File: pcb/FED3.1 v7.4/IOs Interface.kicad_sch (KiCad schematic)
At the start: 29 parts, among them IC1 MC74VHC1GT125DBVT1G, Q2 DMP2035U-7

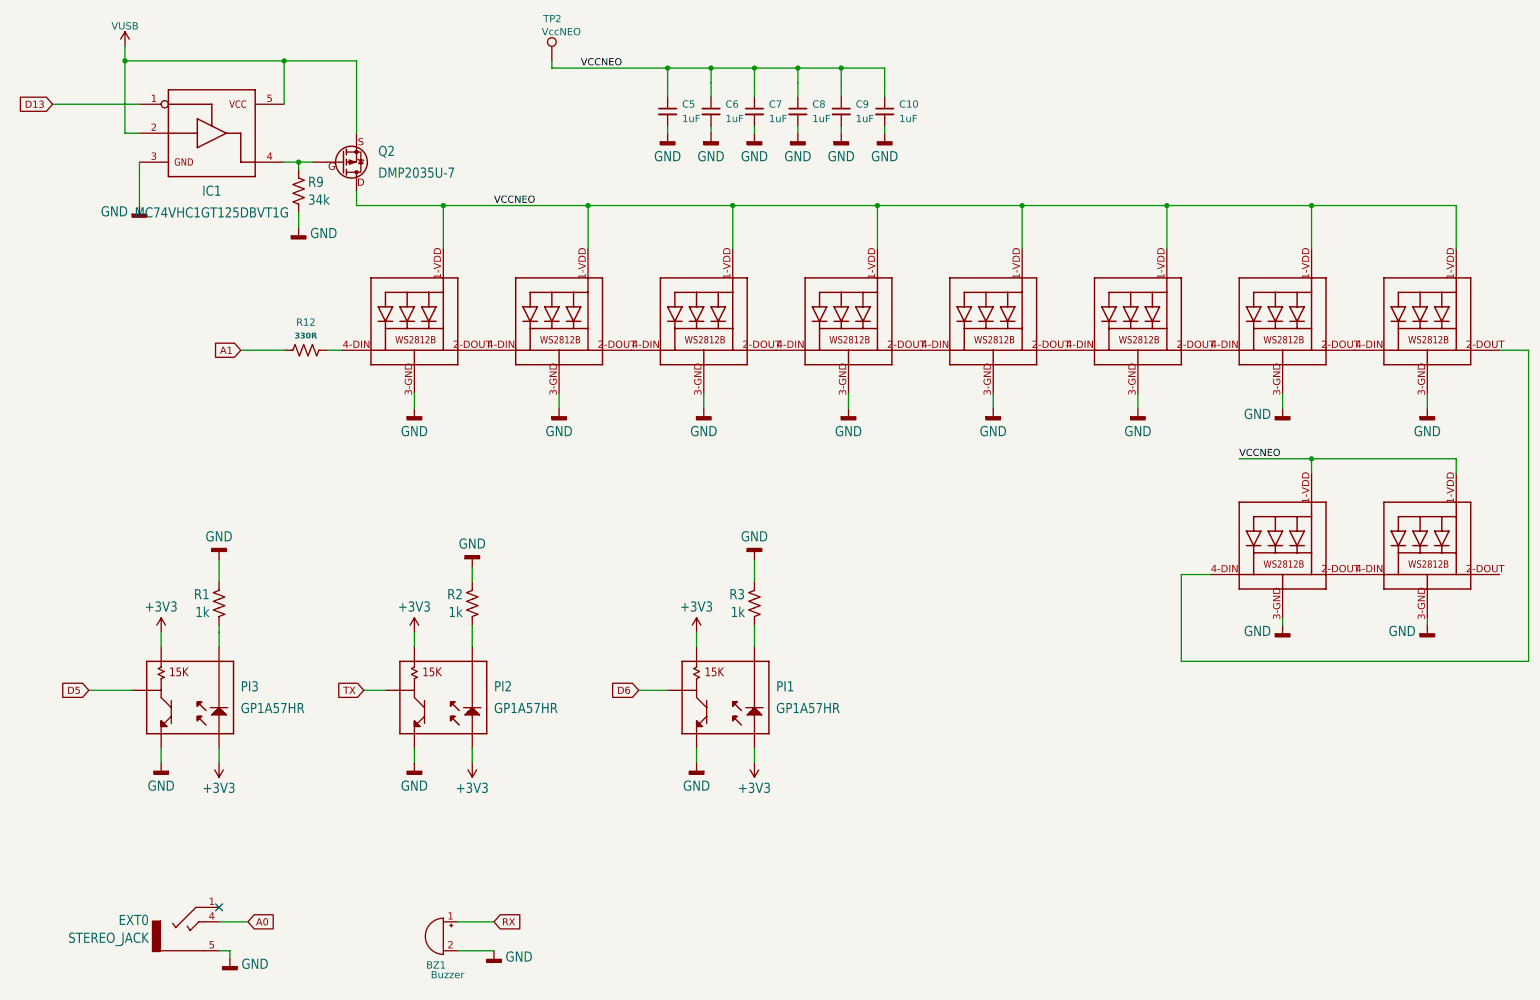
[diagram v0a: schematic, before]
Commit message: review step 2
Realocação de labels e refªs:
- sem qq alteração no circuito
- alteração na PCB apenas a ver com alocação de Designators/SilkScreen parts
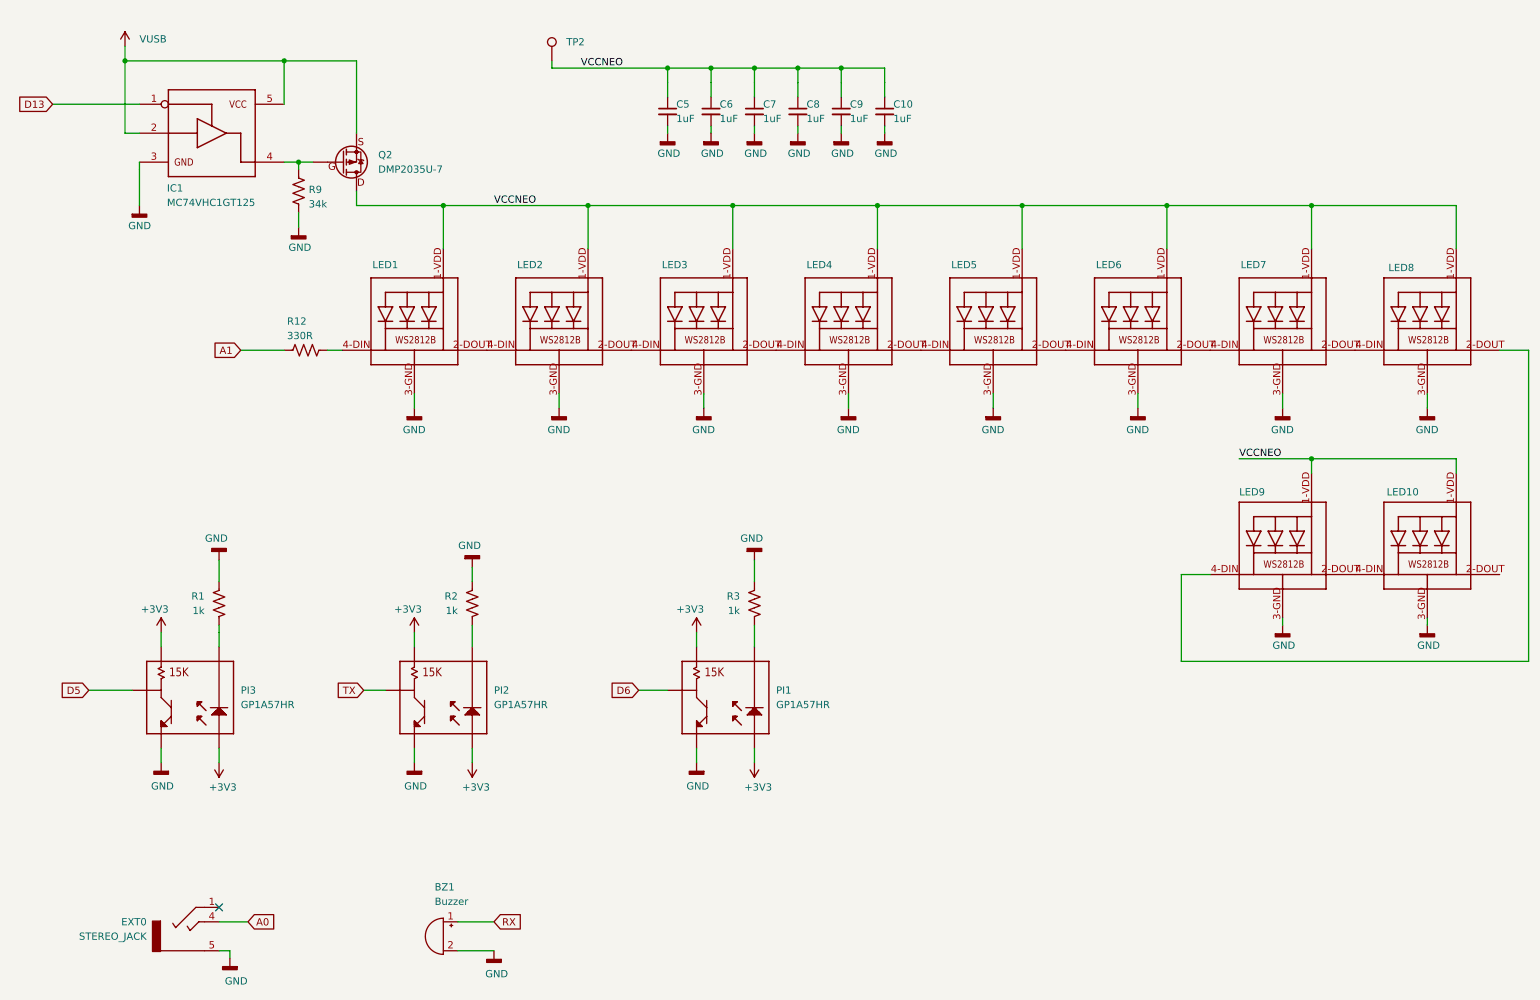
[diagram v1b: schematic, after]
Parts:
- IC1: value MC74VHC1GT125DBVT1G -> MC74VHC1GT125
